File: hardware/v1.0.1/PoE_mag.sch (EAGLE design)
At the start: 130 parts, among them IC1 LD1117V33, IC10 74LVC1T45SOT23-HAND, IC11 74LVC1T45SOT23-HAND, IC12 PCA9517A, IC2 LD1117V33*, IC3 DS1338, IC4 ATMEGA1284, IC5 TSR 1-2450, IC6 LM61, IC7 MCP2200, IC8 74LVC1T45SOT23-HAND, IC9 74LVC1T45SOT23-HAND, Q1 BSS138, Q2 BUK98150-55A, X1 PWR, X2 JTAG, X3 USB, X4 MICRO-SD-SOCKETHIROSE-DM3D, X5 CONN-SMATHD, X6 UFL, X7 22-23-2021, X8 RJ45*, X9 RJ11, Y1 32k768, Y2 12MHz, Y3 12MHz

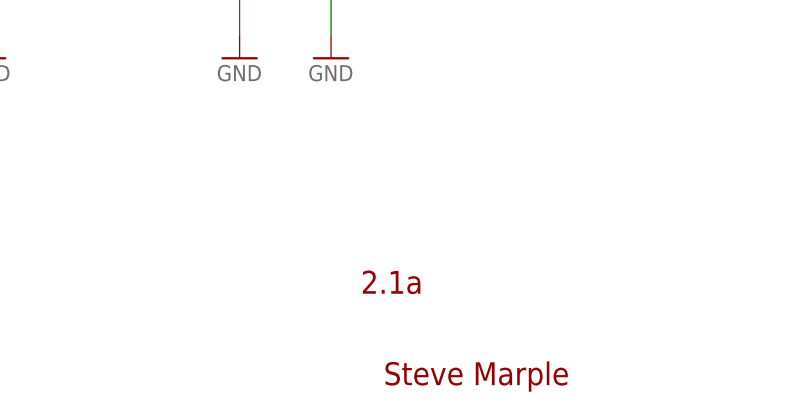
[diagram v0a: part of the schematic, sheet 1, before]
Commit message: Fix incorrect version number on schematic
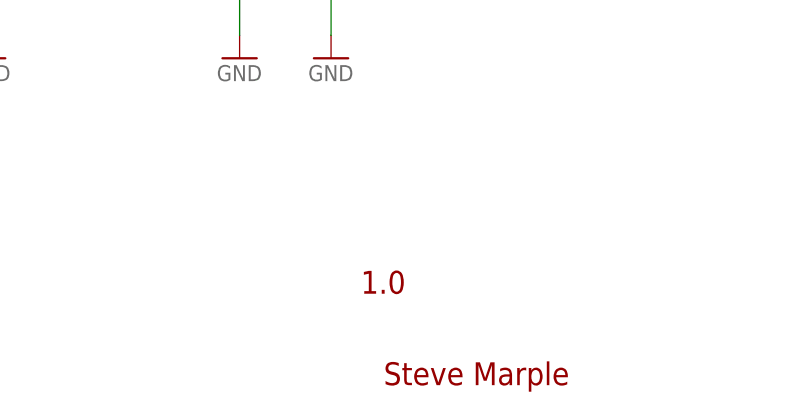
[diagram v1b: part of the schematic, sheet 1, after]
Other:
- note added: "1.0"
- note removed: "2.1a"
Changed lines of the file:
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@@
 <text x="129.54" y="106.68" size="2.54" layer="91">Power LED</text>
 <text x="158.242" y="-71.882" size="2.54" layer="94">Steve Marple</text>
-<text x="155.702" y="-61.722" size="2.54" layer="94">2.1a</text>
+<text x="155.702" y="-61.722" size="2.54" layer="94">1.0</text>
 <text x="-152.4" y="0" size="2.54" layer="91">5V regulator</text>
 <text x="-63.5" y="0" size="1.27" layer="91">Omit load capacitors if resonator</text>
